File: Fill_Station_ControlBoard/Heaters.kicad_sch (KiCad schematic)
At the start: 1 part, among them J1 Conn_01x06

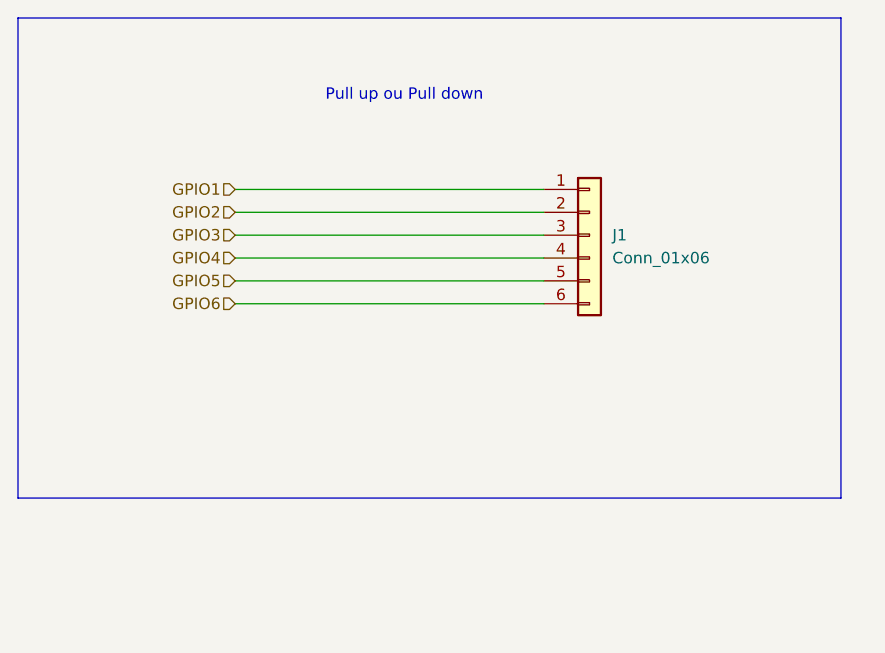
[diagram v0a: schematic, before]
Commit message: Changement de CAN et quelques trucs
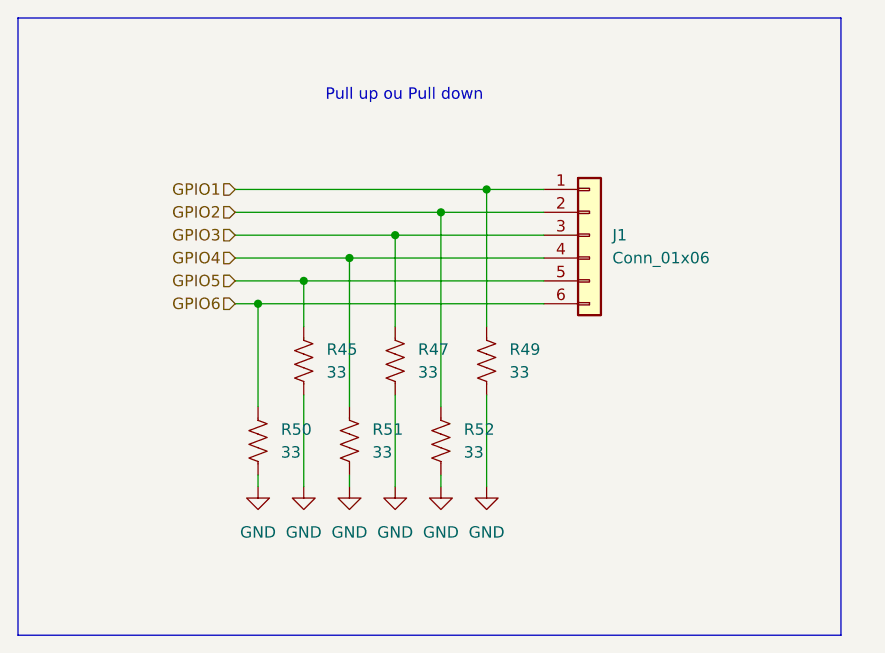
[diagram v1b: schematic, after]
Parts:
- added R45, R47, R49, R50, R51, R52: 33, Resistor_SMD:R_0603_1608Metric_Pad0.98x0.95mm_HandSolder, symbol Device:R_US
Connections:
- net GPIO1: now also R49.2
- net GPIO2: now also R52.2
- net GPIO3: now also R47.2
- net GPIO4: now also R51.2
- net GPIO5: now also R45.2
- net GPIO6: now also R50.2
- new net GND: R45.1, R47.1, R49.1, R50.1, R51.1, R52.1

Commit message: Fait des trucs (commencer arrangement de pièces sur PCB
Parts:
- added D6: 1N4001, Diode_THT:D_DO-41_SOD81_P10.16mm_Horizontal, symbol Diode:1N4001
- added Q1: PMOS_Substrate, symbol Simulation_SPICE:PMOS_Substrate
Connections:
- new net: D6.2 (A), Q1.1 (D)
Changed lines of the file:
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@@
+	(wire
+		(pts
+			(xy 107.95 76.2) (xy 107.95 80.01)
+		)
+		(stroke
+			(width 0)
+			(type default)
+		)
+	)
 	(wire
 		(pts
@@
 	)
 	(symbol
+		(lib_id "Simulation_SPICE:PMOS_Substrate")
+		(at 105.41 85.09 0)
+		(unit 1)
+		(exclude_from_sim no)
+		(in_bom yes)
+		(on_board yes)
+		(dnp no)
+		(fields_autoplaced yes)
+		(property "Reference" "Q1"
+			(at 113.03 83.8199 0)
+			(effects
+				(font
+					(size 1.27 1.27)
+				)
+				(justify left)
+			)
+		)
+		(property "Value" "PMOS_Substrate"
+			(at 113.03 86.3599 0)
+			(effects
+				(font
+					(size 1.27 1.27)
+				)
+				(justify left)
+			)
+		)
+		(property "Footprint" ""
+			(at 146.05 85.09 0)
+			(effects
+				(font
+					(size 1.27 1.27)
+				)
+				(hide yes)
+			)
+		)
+		(property "Datasheet" "https://ngspice.sourceforge.io/docs/ngspice-html-manual/manual.xhtml#cha_MOSFETs"
+			(at 105.41 102.87 0)
+			(effects
+				(font
+					(size 1.27 1.27)
+				)
+				(hide yes)
+			)
+		)
+		(property "Description" "P-channel MOSFET symbol with substrate (bulk) pin"
+			(at 105.41 85.09 0)
+			(effects
+				(font
+					(size 1.27 1.27)
+				)
+				(hide yes)
+			)
+		)
+		(property "Sim.Device" "PMOS"
+			(at 105.41 99.06 0)
+			(effects
+				(font
+					(size 1.27 1.27)
+				)
+				(hide yes)
+			)
+		)
+		(property "Sim.Type" "MOS1"
+			(at 105.41 100.965 0)
+			(effects
+				(font
+					(size 1.27 1.27)
+				)
+				(hide yes)
+			)
+		)
+		(property "Sim.Pins" "1=D 2=G 3=S 4=B"
+			(at 105.41 97.155 0)
+			(effects
+				(font
+					(size 1.27 1.27)
+				)
+				(hide yes)
+			)
+		)
+		(pin "2"
+		)
+		(pin "4"
+		)
+		(pin "3"
+		)
+		(pin "1"
+		)
+		(instances
+			(project ""
+				(path "/eaacffe0-ee57-428e-a37e-5655e0922ccc/8a0f3f8a-bb10-44ee-9a52-010a31de8ac3"
+					(reference "Q1")
+					(unit 1)
+				)
+			)
+		)
+	)
+	(symbol
 		(lib_id "Device:R_US")
 		(at 63.5 78.74 180)
@@
 					(unit 1)
 				)
+			)
+		)
+	)
+	(symbol
+		(lib_id "Diode:1N4001")
+		(at 107.95 72.39 270)
+		(unit 1)
+		(exclude_from_sim no)
+		(in_bom yes)
+		(on_board yes)
+		(dnp no)
+		(fields_autoplaced yes)
+		(property "Reference" "D6"
+			(at 110.49 71.1199 90)
+			(effects
+				(font
+					(size 1.27 1.27)
+				)
+				(justify left)
+			)
+		)
+		(property "Value" "1N4001"
+			(at 110.49 73.6599 90)
+			(effects
+				(font
+					(size 1.27 1.27)
+				)
+				(justify left)
+			)
+		)
+		(property "Footprint" "Diode_THT:D_DO-41_SOD81_P10.16mm_Horizontal"
+			(at 107.95 72.39 0)
+			(effects
+				(font
+					(size 1.27 1.27)
+				)
+				(hide yes)
+			)
+		)
+		(property "Datasheet" "http://www.vishay.com/docs/88503/1n4001.pdf"
+			(at 107.95 72.39 0)
+			(effects
+				(font
+					(size 1.27 1.27)
+				)
+				(hide yes)
+			)
+		)
+		(property "Description" "50V 1A General Purpose Rectifier Diode, DO-41"
+			(at 107.95 72.39 0)
+			(effects
+				(font
+					(size 1.27 1.27)
+				)
+				(hide yes)
+			)
+		)
+		(property "Sim.Device" "D"
+			(at 107.95 72.39 0)
+			(effects
+				(font
+					(size 1.27 1.27)
+				)
+				(hide yes)
+			)
+		)
+		(property "Sim.Pins" "1=K 2=A"
+			(at 107.95 72.39 0)
+			(effects
+				(font
+					(size 1.27 1.27)
+				)
+				(hide yes)
+			)
+		)
+		(pin "2"
+		)
+		(pin "1"
+		)
+		(instances
+			(project ""
+				(path "/eaacffe0-ee57-428e-a37e-5655e0922ccc/8a0f3f8a-bb10-44ee-9a52-010a31de8ac3"
+					(reference "D6")
+					(unit 1)
+				)
